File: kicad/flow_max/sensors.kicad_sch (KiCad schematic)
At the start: 7 parts, among them U1 PAA3905E1, U10 PAT9136E1, U11 BMP390, U12 AFBR-S50LX85D, U4 ICM-45686, U6 VL53L1CXV0FY1, U7 IST8310

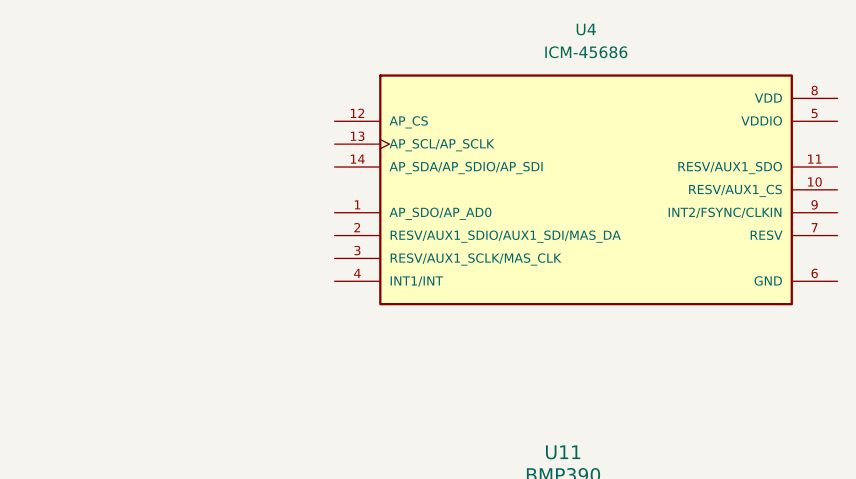
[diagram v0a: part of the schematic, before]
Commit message: Added pin assignment to MCXN947 for the communication lines, Debugger, ISP_Mode and optional GPIO/SD card
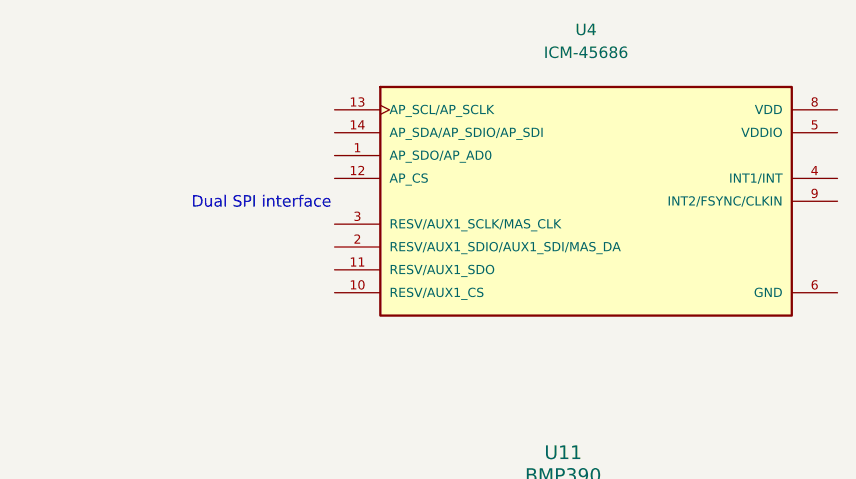
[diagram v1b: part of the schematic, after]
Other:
- note added: "Dual SPI interface"
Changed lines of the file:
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@@
 		(comment 4 "CTO SYSTEM INNOVATIONS / MOBILE ROBOTICS DOMAIN")
+	)
+	(text "Dual SPI interface"
+		(exclude_from_sim no)
+		(at 186.182 57.404 0)
+		(effects
+			(font
+				(size 1.27 1.27)
+			)
+		)
 	)
 	(symbol
